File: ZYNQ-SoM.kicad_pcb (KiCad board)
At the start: 6 copper layers, 50 x 40 mm, 139 parts, among them IC501 TPS51206DSQR, J401 AXK500137YG, J402 AXK500137YG, Q201 MMBT3904, U201 xc7z010clg400, U202 W25Q256FVEI, U301 MT41K256M16TW-107_P, U501 TPS62130ARGTR, U502 TPS62130ARGTR, U503 SPX3819M5-L-3-3, U504 TPS62130ARGTR

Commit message: feat: continue improve sch design
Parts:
- added C315: 10u, Capacitor_SMD:C_0805_2012Metric, F.Cu at (49.1, 78.3)
- added C316: 10u, Capacitor_SMD:C_0805_2012Metric, F.Cu at (49.1, 81.3)
- added C317: 100n, Capacitor_SMD:C_0402_1005Metric, F.Cu at (48.3, 67.9)
- added C318: 100n, Capacitor_SMD:C_0402_1005Metric, F.Cu at (48.3, 69.9)
- added C319: 100n, Capacitor_SMD:C_0402_1005Metric, F.Cu at (48.3, 71.8)
- added C321: 100n, Capacitor_SMD:C_0402_1005Metric, F.Cu at (48.3, 73.8)
- added C322: 100n, Capacitor_SMD:C_0402_1005Metric, F.Cu at (48.3, 75.8)
- added C701: 10u, Capacitor_SMD:C_0805_2012Metric, F.Cu at (4.63, 5.75)
- added C702: 100n, Capacitor_SMD:C_0402_1005Metric, F.Cu at (0.94, 6.46)
- added C703: 100n, Capacitor_SMD:C_0402_1005Metric, F.Cu at (0.94, 8.43)
- added R307: 40R2, Resistor_SMD:R_0402_1005Metric, F.Cu at (29.5, 67.7)
- added R308: 40R2, Resistor_SMD:R_0402_1005Metric, F.Cu at (29.5, 69.7)
- added R309: 40R2, Resistor_SMD:R_0402_1005Metric, F.Cu at (29.5, 71.7)
- added R310: 40R2, Resistor_SMD:R_0402_1005Metric, F.Cu at (29.5, 73.7)
- added R311: 40R2, Resistor_SMD:R_0402_1005Metric, F.Cu at (29.5, 75.7)
- added R312: 40R2, Resistor_SMD:R_0402_1005Metric, F.Cu at (29.5, 77.7)
- added R313: 40R2, Resistor_SMD:R_0402_1005Metric, F.Cu at (29.5, 79.7)
- added R314: 40R2, Resistor_SMD:R_0402_1005Metric, F.Cu at (32.4, 67.7)
- added R315: 40R2, Resistor_SMD:R_0402_1005Metric, F.Cu at (32.4, 69.7)
- added R316: 40R2, Resistor_SMD:R_0402_1005Metric, F.Cu at (32.4, 71.7)
- added R317: 40R2, Resistor_SMD:R_0402_1005Metric, F.Cu at (32.4, 73.7)
- added R318: 40R2, Resistor_SMD:R_0402_1005Metric, F.Cu at (32.4, 75.7)
- added R319: 40R2, Resistor_SMD:R_0402_1005Metric, F.Cu at (32.4, 77.7)
- added R320: 40R2, Resistor_SMD:R_0402_1005Metric, F.Cu at (32.4, 79.7)
- added R321: 40R2, Resistor_SMD:R_0402_1005Metric, F.Cu at (35.3, 67.7)
- added R322: 40R2, Resistor_SMD:R_0402_1005Metric, F.Cu at (35.3, 69.7)
- added R323: 40R2, Resistor_SMD:R_0402_1005Metric, F.Cu at (35.3, 71.7)
- added R324: 40R2, Resistor_SMD:R_0402_1005Metric, F.Cu at (35.3, 73.7)
- added R325: 40R2, Resistor_SMD:R_0402_1005Metric, F.Cu at (35.3, 75.7)
- added R326: 40R2, Resistor_SMD:R_0402_1005Metric, F.Cu at (35.3, 77.7)
- added R327: 40R2, Resistor_SMD:R_0402_1005Metric, F.Cu at (35.3, 79.7)
- added R328: 40R2, Resistor_SMD:R_0402_1005Metric, F.Cu at (38.2, 67.7)
- added R329: 40R2, Resistor_SMD:R_0402_1005Metric, F.Cu at (38.2, 69.7)
- added R330: 40R2, Resistor_SMD:R_0402_1005Metric, F.Cu at (38.2, 71.7)
- added R701: 33R, Resistor_SMD:R_0402_1005Metric, F.Cu at (0.95, 0.49)
- added R702: 33R, Resistor_SMD:R_0402_1005Metric, F.Cu at (0.95, 2.48)
- added R703: 33R, Resistor_SMD:R_0402_1005Metric, F.Cu at (0.95, 4.47)
- added U701: 33.3333MHz, Oscillator:Oscillator_SMD_SeikoEpson_SG8002CE-4Pin_3.2x2.5mm, F.Cu at (5.13, 1.87)
- C201, C202, C522, C524, C526, C528, C530, C532, C536, C538, C539, C541, C542, C544, C547, C549, C551, C552, C554, C555, C556, C558, C559, C560, C562, C563, C564, C565, C566, C568, C569, C570, C571, C572, C573, C574, C575, R202, R203: moved to B.Cu
- FB201: footprint Inductor_SMD:L_0603_1608Metric -> Inductor_SMD:L_0402_1005Metric; moved to B.Cu
- FB501: footprint Inductor_SMD:L_0603_1608Metric -> Inductor_SMD:L_0402_1005Metric
- moved C540 174.3 mm to (222.2, 79.7)
- moved C561 174.3 mm to (222.2, 82.8)
- moved C546 166.0 mm to (210.7, 87.0)
- moved C567 166.0 mm to (210.7, 89.5)
- moved C543 146.0 mm to (171.6, 114.8)
- moved C548 141.5 mm to (171.9, 116.9)
- moved C544 114.8 mm to (159.7, 67.7), turned to 180 degrees
- moved C549 114.0 mm to (160.0, 70.7), turned to 180 degrees
- moved C570 113.8 mm to (140.1, 86.4), turned to 90 degrees
- moved C558 113.4 mm to (137.3, 87.6), turned to 180 degrees
- moved C554 112.8 mm to (136.5, 86.0)
- moved C564 112.0 mm to (138.9, 82.8), turned to 180 degrees
- moved C559 109.0 mm to (139.0, 79.6), turned to 180 degrees
- moved C565 108.0 mm to (140.1, 74.4), turned to -90 degrees
- moved C555 107.0 mm to (135.7, 81.2), turned to 180 degrees
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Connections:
- J401 pad 1: unconnected-(J401-Pad1) -> +VCCIO_34
- J401 pad 2: unconnected-(J401-Pad2) -> +VCCIO_34
- J401 pad 3: unconnected-(J401-Pad3) -> +VCCIO_34
- J401 pad 4: unconnected-(J401-Pad4) -> +VCCIO_34
- J402 pad 1: unconnected-(J402-Pad1) -> +VCCIO_35
- J402 pad 2: unconnected-(J402-Pad2) -> +VCCIO_35
- J402 pad 3: unconnected-(J402-Pad3) -> +VCCIO_35
- J402 pad 4: unconnected-(J402-Pad4) -> +VCCIO_35
- U201 pad A10: unconnected-(U201F-PS_MIO37_501-PadA10) -> OTG_DATA5
- U201 pad A11: unconnected-(U201F-PS_MIO36_501-PadA11) -> OTG_CLK
- U201 pad A12: unconnected-(U201F-PS_MIO34_501-PadA12) -> OTG_DATA2
- U201 pad A14: unconnected-(U201F-PS_MIO32_501-PadA14) -> OTG_DATA0
- U201 pad A15: unconnected-(U201F-PS_MIO26_501-PadA15) -> PS_MIO26
- U201 pad A16: unconnected-(U201F-PS_MIO24_501-PadA16) -> PS_MIO24
- U201 pad A17: unconnected-(U201F-PS_MIO20_501-PadA17) -> PS_MIO20
- U201 pad A19: unconnected-(U201F-PS_MIO16_501-PadA19) -> PS_MIO16
- U201 pad A20: unconnected-(U201D-IO_L2N_T0_AD8N_35-PadA20) -> PL_B35_IO2_N
- U201 pad A5: unconnected-(U201E-PS_MIO6_500-PadA5) -> Net-(U201E-PS_MIO6_500)
- U201 pad A6: unconnected-(U201E-PS_MIO5_500-PadA6) -> QSPI_D3_PS_MIO5
- U201 pad A7: unconnected-(U201E-PS_MIO1_500-PadA7) -> QSPI_CS
- U201 pad A9: unconnected-(U201F-PS_MIO43_501-PadA9) -> SD_DATA1
- U201 pad B10: unconnected-(U201F-PS_SRST_B_501-PadB10) -> PS_SRST_B
- U201 pad B12: unconnected-(U201F-PS_MIO48_501-PadB12) -> PS_MIO48
- U201 pad B13: unconnected-(U201F-PS_MIO50_501-PadB13) -> PS_MIO50
- U201 pad B14: unconnected-(U201F-PS_MIO47_501-PadB14) -> PS_MIO47
- U201 pad B15: unconnected-(U201F-PS_MIO45_501-PadB15) -> SD_DATA3
- U201 pad B17: unconnected-(U201F-PS_MIO22_501-PadB17) -> PS_MIO22
- U201 pad B18: unconnected-(U201F-PS_MIO18_501-PadB18) -> PS_MIO18
- U201 pad B19: unconnected-(U201D-IO_L2P_T0_AD8P_35-PadB19) -> PL_B35_IO2_P
- U201 pad B20: unconnected-(U201D-IO_L1N_T0_AD0N_35-PadB20) -> PL_B35_IO1_N
- U201 pad B5: unconnected-(U201E-PS_MIO9_500-PadB5) -> PS_MIO9
- U201 pad B6: Net-(U201E-VCCO_MIO0_500[2]-PadB6) -> +3V3
- U201 pad B7: unconnected-(U201E-PS_MIO4_500-PadB7) -> QSPI_D2_PS_MIO4
- U201 pad B8: unconnected-(U201E-PS_MIO2_500-PadB8) -> QSPI_D0
- U201 pad B9: unconnected-(U201F-PS_MIO51_501-PadB9) -> PS_MIO51
- U201 pad C10: unconnected-(U201F-PS_MIO52_501-PadC10) -> PS_MIO52
- U201 pad C11: unconnected-(U201F-PS_MIO53_501-PadC11) -> PS_MIO53
- U201 pad C12: unconnected-(U201F-PS_MIO49_501-PadC12) -> PS_MIO49
- U201 pad C13: unconnected-(U201F-PS_MIO29_501-PadC13) -> OTG_DIR
- U201 pad C15: unconnected-(U201F-PS_MIO30_501-PadC15) -> OTG_STP
- U201 pad C16: unconnected-(U201F-PS_MIO28_501-PadC16) -> OTG_DATA4
- U201 pad C17: unconnected-(U201F-PS_MIO41_501-PadC17) -> SD_CMD
- U201 pad C18: unconnected-(U201F-PS_MIO39_501-PadC18) -> OTG_DATA7
- U201 pad C20: unconnected-(U201D-IO_L1P_T0_AD0P_35-PadC20) -> PL_B35_IO1_P
- U201 pad C5: unconnected-(U201E-PS_MIO14_500-PadC5) -> UART_RX
- U201 pad C6: unconnected-(U201E-PS_MIO11_500-PadC6) -> PS_MIO11
- U201 pad C7: unconnected-(U201E-PS_POR_B_500-PadC7) -> PS_POR_B
- U201 pad C8: unconnected-(U201E-PS_MIO15_500-PadC8) -> UART_TX
- U201 pad D10: unconnected-(U201F-PS_MIO19_501-PadD10) -> PS_MIO19
- U201 pad D11: unconnected-(U201F-PS_MIO23_501-PadD11) -> PS_MIO23
- U201 pad D13: unconnected-(U201F-PS_MIO27_501-PadD13) -> PS_MIO27
- U201 pad D14: unconnected-(U201F-PS_MIO40_501-PadD14) -> Net-(U201F-PS_MIO40_501)
- U201 pad D15: unconnected-(U201F-PS_MIO33_501-PadD15) -> OTG_DATA1
- U201 pad D16: unconnected-(U201F-PS_MIO46_501-PadD16) -> OTG_nRST
- U201 pad D18: unconnected-(U201D-IO_L3N_T0_DQS_AD1N_35-PadD18) -> PL_B35_IO3_N
- U201 pad D19: unconnected-(U201D-IO_L4P_T0_35-PadD19) -> PL_B35_IO4_P
- U201 pad D20: unconnected-(U201D-IO_L4N_T0_35-PadD20) -> PL_B35_IO4_N
- U201 pad D5: unconnected-(U201E-PS_MIO8_500-PadD5) -> PS_MIO8
- U201 pad D6: unconnected-(U201E-PS_MIO3_500-PadD6) -> QSPI_D1
- U201 pad D7: Net-(U201E-VCCO_MIO0_500[2]-PadB6) -> +3V3
- U201 pad D8: unconnected-(U201E-PS_MIO7_500-PadD8) -> PS_MIO7
- U201 pad D9: unconnected-(U201E-PS_MIO12_500-PadD9) -> PS_MIO12
- U201 pad E11: unconnected-(U201F-PS_MIO_VREF_501-PadE11) -> PS_MIO_VREF
- U201 pad E12: unconnected-(U201F-PS_MIO42_501-PadE12) -> SD_DATA0
- U201 pad E13: unconnected-(U201F-PS_MIO38_501-PadE13) -> OTG_DATA6
- U201 pad E14: unconnected-(U201F-PS_MIO17_501-PadE14) -> PS_MIO17
- U201 pad E16: unconnected-(U201F-PS_MIO31_501-PadE16) -> OTG_NXT
- U201 pad E17: unconnected-(U201D-IO_L3P_T0_DQS_AD1P_35-PadE17) -> PL_B35_IO3_P
- U201 pad E18: unconnected-(U201D-IO_L5P_T0_AD9P_35-PadE18) -> PL_B35_IO5_P
- U201 pad E19: unconnected-(U201D-IO_L5N_T0_AD9N_35-PadE19) -> PL_B35_IO5_N
- U201 pad E6: unconnected-(U201E-PS_MIO0_500-PadE6) -> PS_MIO0
- U201 pad E7: unconnected-(U201E-PS_CLK_500-PadE7) -> Net-(U201E-PS_CLK_500)
- U201 pad E8: unconnected-(U201E-PS_MIO13_500-PadE8) -> PS_MIO13
- U201 pad E9: unconnected-(U201E-PS_MIO10_500-PadE9) -> PS_MIO10
- U201 pad F12: unconnected-(U201F-PS_MIO35_501-PadF12) -> OTG_DATA3
- U201 pad F13: unconnected-(U201F-PS_MIO44_501-PadF13) -> SD_DATA2
- U201 pad F14: unconnected-(U201F-PS_MIO21_501-PadF14) -> PS_MIO21
- U201 pad F15: unconnected-(U201F-PS_MIO25_501-PadF15) -> PS_MIO25
- U201 pad F16: unconnected-(U201D-IO_L6P_T0_35-PadF16) -> PL_B35_IO6_P
- U201 pad F17: unconnected-(U201D-IO_L6N_T0_VREF_35-PadF17) -> PL_B35_IO6_N
- U201 pad F19: unconnected-(U201D-IO_L15P_T2_DQS_AD12P_35-PadF19) -> PL_B35_IO15_P
- U201 pad F20: unconnected-(U201D-IO_L15N_T2_DQS_AD12N_35-PadF20) -> PL_B35_IO15_N
- U201 pad G14: unconnected-(U201D-IO_0_35-PadG14) -> PL_B35_IO0
- U201 pad G15: unconnected-(U201D-IO_L19N_T3_VREF_35-PadG15) -> PL_B35_IO19_N
- U201 pad G17: unconnected-(U201D-IO_L16P_T2_35-PadG17) -> PL_B35_IO16_P
- U201 pad G18: unconnected-(U201D-IO_L16N_T2_35-PadG18) -> PL_B35_IO16_N
- U201 pad G19: unconnected-(U201D-IO_L18P_T2_AD13P_35-PadG19) -> PL_B35_IO18_P
- U201 pad G20: unconnected-(U201D-IO_L18N_T2_AD13N_35-PadG20) -> PL_B35_IO18_N
- U201 pad H15: unconnected-(U201D-IO_L19P_T3_35-PadH15) -> PL_B35_IO19_P
- U201 pad H16: unconnected-(U201D-IO_L13P_T2_MRCC_35-PadH16) -> PL_B35_IO13_P
- U201 pad H17: unconnected-(U201D-IO_L13N_T2_MRCC_35-PadH17) -> PL_B35_IO13_N
- U201 pad H18: unconnected-(U201D-IO_L14N_T2_AD4N_SRCC_35-PadH18) -> PL_B35_IO14_N
- U201 pad H20: unconnected-(U201D-IO_L17N_T2_AD5N_35-PadH20) -> PL_B35_IO17_N
- U201 pad J14: unconnected-(U201D-IO_L20N_T3_AD6N_35-PadJ14) -> PL_B35_IO20_N
- U201 pad J15: unconnected-(U201D-IO_25_35-PadJ15) -> PL_B35_IO25
- U201 pad J16: unconnected-(U201D-IO_L24N_T3_AD15N_35-PadJ16) -> PL_B35_IO24_N
- U201 pad J18: unconnected-(U201D-IO_L14P_T2_AD4P_SRCC_35-PadJ18) -> PL_B35_IO14_P
- U201 pad J19: unconnected-(U201D-IO_L10N_T1_AD11N_35-PadJ19) -> PL_B35_IO10_N
- U201 pad J20: unconnected-(U201D-IO_L17P_T2_AD5P_35-PadJ20) -> PL_B35_IO17_P
- U201 pad K14: unconnected-(U201D-IO_L20P_T3_AD6P_35-PadK14) -> PL_B35_IO20_P
- U201 pad K16: unconnected-(U201D-IO_L24P_T3_AD15P_35-PadK16) -> PL_B35_IO24_P
- U201 pad K17: unconnected-(U201D-IO_L12P_T1_MRCC_35-PadK17) -> PL_B35_IO12_P
- U201 pad K18: unconnected-(U201D-IO_L12N_T1_MRCC_35-PadK18) -> PL_B35_IO12_N
- U201 pad K19: unconnected-(U201D-IO_L10P_T1_AD11P_35-PadK19) -> PL_B35_IO10_P
- U201 pad L14: unconnected-(U201D-IO_L22P_T3_AD7P_35-PadL14) -> PL_B35_IO22_P
- U201 pad L15: unconnected-(U201D-IO_L22N_T3_AD7N_35-PadL15) -> PL_B35_IO22_N
- U201 pad L16: unconnected-(U201D-IO_L11P_T1_SRCC_35-PadL16) -> PL_B35_IO11_P
- U201 pad L17: unconnected-(U201D-IO_L11N_T1_SRCC_35-PadL17) -> PL_B35_IO11_N
- U201 pad L19: unconnected-(U201D-IO_L9P_T1_DQS_AD3P_35-PadL19) -> PL_B35_IO9_P
- U201 pad L20: unconnected-(U201D-IO_L9N_T1_DQS_AD3N_35-PadL20) -> PL_B35_IO9_N
- U201 pad M14: unconnected-(U201D-IO_L23P_T3_35-PadM14) -> PL_B35_IO23_P
- U201 pad M15: unconnected-(U201D-IO_L23N_T3_35-PadM15) -> PL_B35_IO23_N
- U201 pad M17: unconnected-(U201D-IO_L8P_T1_AD10P_35-PadM17) -> PL_B35_IO8_P
- U201 pad M18: unconnected-(U201D-IO_L8N_T1_AD10N_35-PadM18) -> PL_B35_IO8_N
- U201 pad M19: unconnected-(U201D-IO_L7P_T1_AD2P_35-PadM19) -> PL_B35_IO7_P
- U201 pad M20: unconnected-(U201D-IO_L7N_T1_AD2N_35-PadM20) -> PL_B35_IO7_N
- U201 pad N15: unconnected-(U201D-IO_L21P_T3_DQS_AD14P_35-PadN15) -> PL_B35_IO21_P
- U201 pad N16: unconnected-(U201D-IO_L21N_T3_DQS_AD14N_35-PadN16) -> PL_B35_IO21_N
- U201 pad N17: unconnected-(U201C-IO_L23P_T3_34-PadN17) -> PL_B34_IO23_P
- U201 pad N18: unconnected-(U201C-IO_L13P_T2_MRCC_34-PadN18) -> PL_B34_IO13_P
- U201 pad N20: unconnected-(U201C-IO_L14P_T2_SRCC_34-PadN20) -> PL_B34_IO14_P
- U201 pad P14: unconnected-(U201C-IO_L6P_T0_34-PadP14) -> PL_B34_IO6_P
- U201 pad P15: unconnected-(U201C-IO_L24P_T3_34-PadP15) -> PL_B34_IO24_P
- U201 pad P16: unconnected-(U201C-IO_L24N_T3_34-PadP16) -> PL_B34_IO24_N
- U201 pad P18: unconnected-(U201C-IO_L23N_T3_34-PadP18) -> PL_B34_IO23_N
- U201 pad P19: unconnected-(U201C-IO_L13N_T2_MRCC_34-PadP19) -> PL_B34_IO13_N
- U201 pad P20: unconnected-(U201C-IO_L14N_T2_SRCC_34-PadP20) -> PL_B34_IO14_N
- U201 pad R14: unconnected-(U201C-IO_L6N_T0_VREF_34-PadR14) -> PL_B34_IO6_N
- U201 pad R16: unconnected-(U201C-IO_L19P_T3_34-PadR16) -> PL_B34_IO19_P
- U201 pad R17: unconnected-(U201C-IO_L19N_T3_VREF_34-PadR17) -> PL_B34_IO19_N
- U201 pad R18: unconnected-(U201C-IO_L20N_T3_34-PadR18) -> PL_B34_IO20_N
- U201 pad R19: unconnected-(U201C-IO_0_34-PadR19) -> PL_B34_IO0
- U201 pad T10: unconnected-(U201C-IO_L1N_T0_34-PadT10) -> PL_B34_IO1_N
- U201 pad T11: unconnected-(U201C-IO_L1P_T0_34-PadT11) -> PL_B34_IO1_P
- U201 pad T12: unconnected-(U201C-IO_L2P_T0_34-PadT12) -> PL_B34_IO2_P
- U201 pad T14: unconnected-(U201C-IO_L5P_T0_34-PadT14) -> PL_B34_IO5_P
- U201 pad T15: unconnected-(U201C-IO_L5N_T0_34-PadT15) -> PL_B34_IO5_N
- U201 pad T16: unconnected-(U201C-IO_L9P_T1_DQS_34-PadT16) -> PL_B34_IO9_P
- U201 pad T17: unconnected-(U201C-IO_L20P_T3_34-PadT17) -> PL_B34_IO20_P
- U201 pad T19: unconnected-(U201C-IO_25_34-PadT19) -> PL_B34_IO25
- U201 pad T20: unconnected-(U201C-IO_L15P_T2_DQS_34-PadT20) -> PL_B34_IO15_P
- U201 pad U12: unconnected-(U201C-IO_L2N_T0_34-PadU12) -> PL_B34_IO2_N
- U201 pad U13: unconnected-(U201C-IO_L3P_T0_DQS_PUDC_B_34-PadU13) -> PL_B34_IO3_P
- U201 pad U14: unconnected-(U201C-IO_L11P_T1_SRCC_34-PadU14) -> PL_B34_IO11_P
- U201 pad U15: unconnected-(U201C-IO_L11N_T1_SRCC_34-PadU15) -> PL_B34_IO11_N
- U201 pad U17: unconnected-(U201C-IO_L9N_T1_DQS_34-PadU17) -> PL_B34_IO9_N
- U201 pad U18: unconnected-(U201C-IO_L12P_T1_MRCC_34-PadU18) -> PL_B34_IO12_P
- U201 pad U19: unconnected-(U201C-IO_L12N_T1_MRCC_34-PadU19) -> PL_B34_IO12_N
- U201 pad U20: unconnected-(U201C-IO_L15N_T2_DQS_34-PadU20) -> PL_B34_IO15_N
- U201 pad V12: unconnected-(U201C-IO_L4P_T0_34-PadV12) -> PL_B34_IO4_P
- U201 pad V13: unconnected-(U201C-IO_L3N_T0_DQS_34-PadV13) -> PL_B34_IO3_N
- U201 pad V15: unconnected-(U201C-IO_L10P_T1_34-PadV15) -> PL_B34_IO10_P
- U201 pad V16: unconnected-(U201C-IO_L18P_T2_34-PadV16) -> PL_B34_IO18_P
- U201 pad V17: unconnected-(U201C-IO_L21P_T3_DQS_34-PadV17) -> PL_B34_IO21_P
- U201 pad V18: unconnected-(U201C-IO_L21N_T3_DQS_34-PadV18) -> PL_B34_IO21_N
- U201 pad V20: unconnected-(U201C-IO_L16P_T2_34-PadV20) -> PL_B34_IO16_P
- U201 pad W13: unconnected-(U201C-IO_L4N_T0_34-PadW13) -> PL_B34_IO4_N
- U201 pad W14: unconnected-(U201C-IO_L8P_T1_34-PadW14) -> PL_B34_IO8_P
- U201 pad W15: unconnected-(U201C-IO_L10N_T1_34-PadW15) -> PL_B34_IO10_N
- U201 pad W16: unconnected-(U201C-IO_L18N_T2_34-PadW16) -> PL_B34_IO18_N
- U201 pad W18: unconnected-(U201C-IO_L22P_T3_34-PadW18) -> PL_B34_IO22_P
- U201 pad W19: unconnected-(U201C-IO_L22N_T3_34-PadW19) -> PL_B34_IO22_N
- U201 pad W20: unconnected-(U201C-IO_L16N_T2_34-PadW20) -> PL_B34_IO16_N
- U201 pad Y14: unconnected-(U201C-IO_L8N_T1_34-PadY14) -> PL_B34_IO8_N
- U201 pad Y16: unconnected-(U201C-IO_L7P_T1_34-PadY16) -> PL_B34_IO7_P
- U201 pad Y17: unconnected-(U201C-IO_L7N_T1_34-PadY17) -> PL_B34_IO7_N
- U201 pad Y18: unconnected-(U201C-IO_L17P_T2_34-PadY18) -> PL_B34_IO17_P
- U201 pad Y19: unconnected-(U201C-IO_L17N_T2_34-PadY19) -> PL_B34_IO17_N
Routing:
- net GND: track 0.00 -> 1.70 mm, vias 0 -> 60
- net unconnected-(J402-Pad31): track 0.00 -> 1.40 mm, vias 0 -> 1
- net unconnected-(J402-Pad29): track 0.00 -> 1.40 mm, vias 0 -> 1
- net unconnected-(J402-Pad27): track 0.00 -> 1.40 mm, vias 0 -> 1
- net unconnected-(J402-Pad25): track 0.00 -> 1.40 mm, vias 0 -> 1
- net unconnected-(J402-Pad23): track 0.00 -> 1.40 mm, vias 0 -> 1
- net unconnected-(J402-Pad21): track 0.00 -> 1.40 mm, vias 0 -> 1
- net unconnected-(J402-Pad19): track 0.00 -> 1.40 mm, vias 0 -> 1
- net unconnected-(J402-Pad17): track 0.00 -> 1.40 mm, vias 0 -> 1
- net unconnected-(J402-Pad15): track 0.00 -> 1.40 mm, vias 0 -> 1
- net unconnected-(J402-Pad13): track 0.00 -> 1.40 mm, vias 0 -> 1
- net unconnected-(J402-Pad11): track 0.00 -> 1.40 mm, vias 0 -> 1
- net unconnected-(J402-Pad9): track 0.00 -> 1.40 mm, vias 0 -> 1
- net unconnected-(J402-Pad7): track 0.00 -> 1.40 mm, vias 0 -> 1
- net unconnected-(J402-Pad5): track 0.00 -> 1.40 mm, vias 0 -> 1
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
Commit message: feat: basic power layout
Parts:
- moved L502 72.5 mm to (116.4, 88.9)
- moved U502 72.5 mm to (118.2, 96.2)
- moved C506 70.7 mm to (119.7, 94.1), turned to 90 degrees
- moved L503 70.6 mm to (135.0, 92.7)
- moved U504 70.4 mm to (140.9, 95.0)
- moved R507 69.5 mm to (138.8, 91.4)
- moved R509 69.5 mm to (142.8, 91.4)
- moved R508 69.5 mm to (140.8, 91.4)
- moved C514 67.6 mm to (131.1, 91.9)
- moved C516 67.6 mm to (131.1, 93.9)
- moved C504 67.2 mm to (116.2, 97.9), turned to 180 degrees
- moved C534 66.3 mm to (136.8, 96.1)
- moved C512 65.7 mm to (132.9, 96.5)
- moved C502 65.6 mm to (118.3, 92.4)
- moved R502 63.5 mm to (114.7, 94.0)
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
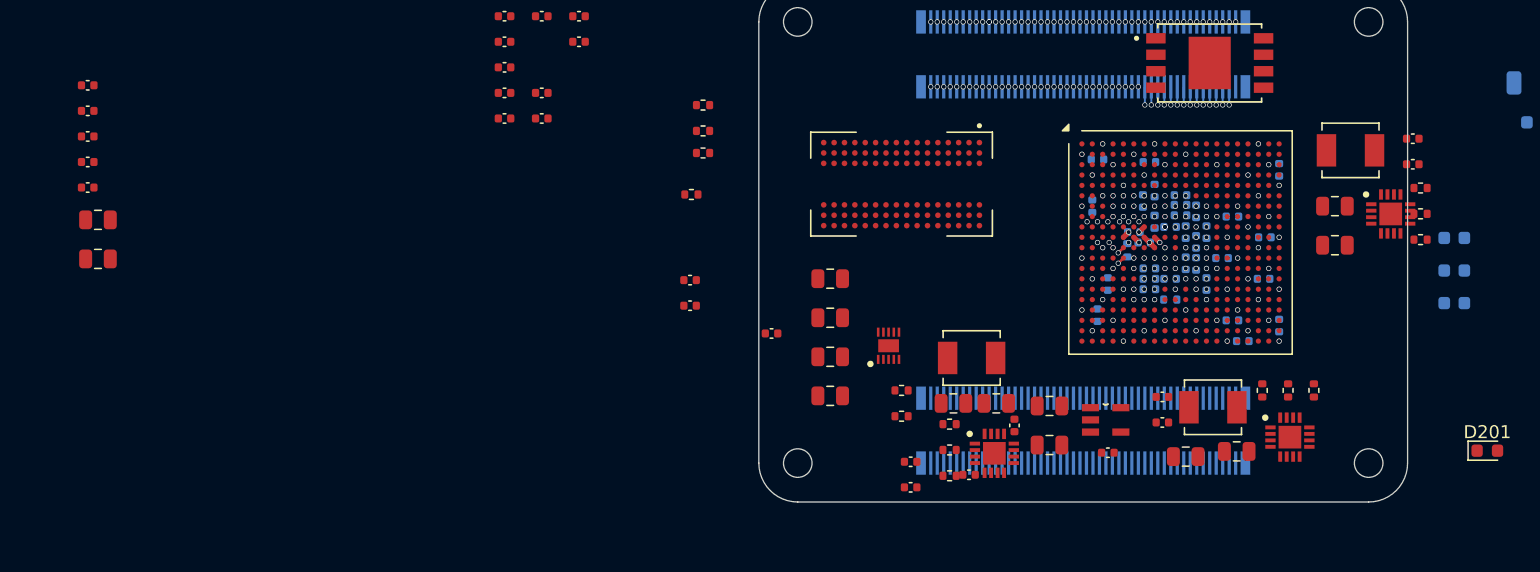
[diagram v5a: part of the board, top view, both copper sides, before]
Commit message: feat: finish basic ddr3 routing
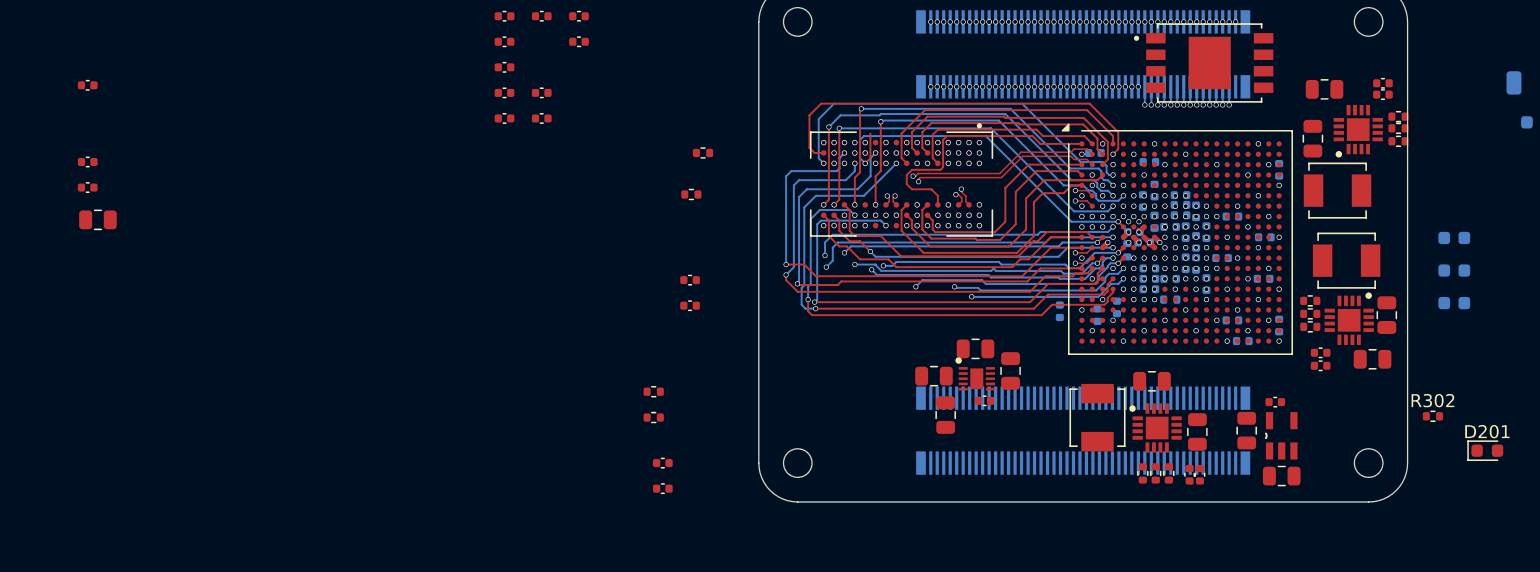
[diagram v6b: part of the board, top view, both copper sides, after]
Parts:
- removed C316: 10u, Capacitor_SMD:C_0805_2012Metric
- removed C318, C319: 100n, Capacitor_SMD:C_0402_1005Metric
- removed R303: 10k, Resistor_SMD:R_0402_1005Metric
- R302: value 10k -> 4k7
- moved R302 61.2 mm to (152.0, 93.4)
- moved C311 19.1 mm to (92.6, 97.0)
- moved C313 19.1 mm to (92.6, 99.0)
- moved R305 19.1 mm to (91.9, 91.5)
- moved R306 19.1 mm to (91.9, 93.5)
- moved C509 18.7 mm to (140.3, 98.0)
- moved C535 17.2 mm to (117.4, 92.2), turned to 180 degrees
- moved C504 17.0 mm to (133.2, 97.9), turned to -90 degrees
- moved R506 16.9 mm to (131.6, 97.8), turned to -90 degrees
- moved C512 16.2 mm to (147.3, 89.0)
- moved R505 16.0 mm to (130.6, 97.8), turned to 90 degrees
- moved C502 15.7 mm to (133.8, 94.6), turned to -90 degrees
- moved C534 15.6 mm to (148.4, 85.6), turned to -90 degrees
- moved C511 15.4 mm to (130.3, 90.7)
- moved R502 15.4 mm to (129.6, 97.8), turned to 90 degrees
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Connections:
- C301 pad 2: VTTREF -> +VTTREF
- C302 pad 1: VTTREF -> +VTTREF
- J401 pad 10: unconnected-(J401-Pad10) -> +5V
- J401 pad 11: unconnected-(J401-Pad11) -> +5V
- J401 pad 12: unconnected-(J401-Pad12) -> +5V
- J401 pad 5: unconnected-(J401-Pad5) -> GND
- J401 pad 6: unconnected-(J401-Pad6) -> GND
- J401 pad 7: unconnected-(J401-Pad7) -> +5V
- J401 pad 8: unconnected-(J401-Pad8) -> +5V
- J401 pad 9: unconnected-(J401-Pad9) -> +5V
- R302 pad 1: +1V5 -> /DDR3/DDR_~{RESET}
- R302 pad 2: VTTREF -> GND
- U301 pad A7: /DDR3/DDR_D13 -> /DDR3/DDR_D14
- U301 pad B8: /DDR3/DDR_D15 -> /DDR3/DDR_D13
- U301 pad C3: /DDR3/DDR_D11 -> /DDR3/DDR_D12
- U301 pad C8: /DDR3/DDR_D12 -> /DDR3/DDR_D15
- U301 pad D7: /DDR3/DDR_D14 -> /DDR3/DDR_D11
- U301 pad F2: /DDR3/DDR_D0 -> /DDR3/DDR_D1
- U301 pad F7: /DDR3/DDR_D7 -> /DDR3/DDR_D5
- U301 pad F8: /DDR3/DDR_D1 -> /DDR3/DDR_D6
- U301 pad G2: /DDR3/DDR_D6 -> /DDR3/DDR_D0
- U301 pad H1: VTTREF -> +VTTREF
- U301 pad H3: /DDR3/DDR_D5 -> /DDR3/DDR_D3
- U301 pad H7: /DDR3/DDR_D4 -> /DDR3/DDR_D7
- U301 pad H8: /DDR3/DDR_D3 -> /DDR3/DDR_D4
- U301 pad M8: VTTREF -> +VTTREF
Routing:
- net /DDR3/DDR_~{RAS}: track 0.00 -> 41.5 mm, vias 0 -> 2
- net /DDR3/DDR_A0: track 0.00 -> 38.0 mm, vias 0 -> 2
- net /DDR3/DDR_~{CS}: track 0.00 -> 37.4 mm, vias 0 -> 2
- net /DDR3/DDR_A5: track 0.00 -> 36.6 mm, vias 0 -> 2
- net /DDR3/DDR_BA1: track 0.00 -> 35.8 mm, vias 0 -> 2
- net /DDR3/DDR_A7: track 0.00 -> 35.5 mm, vias 1 -> 3
- net /DDR3/DDR_CKE: track 0.00 -> 35.3 mm, vias 0 -> 2
- net /DDR3/DDR_A9: track 0.00 -> 33.3 mm, vias 1 -> 3
- net /DDR3/DDR_A14: track 0.00 -> 31.3 mm, vias 1 -> 3
- net /DDR3/DDR_~{RESET}: track 0.00 -> 30.7 mm, vias 0 -> 1
- net /DDR3/DDR_A2: track 0.00 -> 30.6 mm, vias 0 -> 3
- net /DDR3/DDR_A11: track 0.00 -> 30.0 mm, vias 1 -> 3
- net /DDR3/DDR_A12: track 0.00 -> 29.7 mm, vias 0 -> 3
- net /DDR3/DDR_ODT: track 0.00 -> 29.7 mm, vias 0 -> 3
- net /DDR3/DDR_BA0: track 0.57 -> 30.1 mm, vias 1 -> 3
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
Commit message: feat: need finish power layout
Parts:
- moved C509 6.96 mm to (145.4, 93.3), turned to 90 degrees
- moved C519 4.93 mm to (142.3, 95.9), turned to 0 degrees
- moved C529 4.00 mm to (115.2, 93.9)
- moved C531 4.00 mm to (116.2, 96.9)
- moved C513 4.00 mm to (118.5, 91.8)
- moved C515 4.00 mm to (121.2, 93.5)
- moved C535 4.00 mm to (119.2, 95.8)
- moved IC501 4.00 mm to (118.5, 94.1)
- moved C504 3.57 mm to (135.7, 95.3), turned to 0 degrees
- moved U503 2.59 mm to (142.3, 93.3), turned to 180 degrees
- moved C506 2.37 mm to (135.7, 96.2), turned to 180 degrees
- moved R503 2.34 mm to (148.5, 72.5)
- moved R504 2.34 mm to (148.5, 73.4)
- moved C502 2.33 mm to (135.7, 93.2), turned to 90 degrees
- moved C503 2.28 mm to (145.9, 69.2), turned to 90 degrees
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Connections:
- J401 pad 86: unconnected-(J401-Pad86) -> PL_B34_IO8_N
- J401 pad 88: unconnected-(J401-Pad88) -> PL_B34_IO8_P
- J401 pad 92: unconnected-(J401-Pad92) -> PL_B34_IO4_N
- J401 pad 94: unconnected-(J401-Pad94) -> PL_B34_IO4_P
- J401 pad 96: unconnected-(J401-Pad96) -> PL_B34_IO1_P
- J401 pad 98: unconnected-(J401-Pad98) -> PL_B34_IO1_N
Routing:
- net PL_B34_IO1_P: track 0.00 -> 25.0 mm, vias 0 -> 1
- net PL_B34_IO1_N: track 0.00 -> 24.7 mm, vias 0 -> 1
- net PL_B34_IO4_P: track 0.00 -> 23.7 mm, vias 0 -> 1
- net PL_B34_IO4_N: track 0.00 -> 23.1 mm, vias 0 -> 1
- net PL_B34_IO8_P: track 0.00 -> 23.0 mm, vias 0 -> 1
- net PL_B34_IO8_N: track 0.00 -> 22.1 mm, vias 0 -> 1
- net /DDR3/DDR_A5: track 36.6 -> 33.1 mm
- net /DDR3/DDR_BA2: track 27.8 -> 25.3 mm
- net /DDR3/DDR_BA1: track 35.8 -> 33.4 mm
- net /DDR3/DDR_CKE: track 35.3 -> 33.6 mm
- net /DDR3/DDR_~{RAS}: track 41.5 -> 40.2 mm
- net /DDR3/DDR_A0: track 38.0 -> 36.9 mm
- net /DDR3/DDR_~{CS}: track 37.4 -> 36.3 mm
